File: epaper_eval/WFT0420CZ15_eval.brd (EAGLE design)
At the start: 47 x 47 mm, 15 parts, among them CN1 WFT0420CZ15_IF, CN2 WFT0420CZ15

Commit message: 部品を追加
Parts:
- added C10, C12: 1uF50V, Parts:SMD_2012
- added C11: 4.7uF50V, Parts:SMD_2012
- added C13: 0.1uF, Parts:SMD_2012
- added D1, D2, D3: MBR0530, Parts:MBR0530
- added L1: 10uH, Parts:NLCV25T
- added Q1: SI1308EDL, Parts:SOT323
- added R1: 0.47, Parts:SMD_2012
- added R2, R3: 4.7k, Parts:SMD_2012
- added U1: LM75BIMM-3, Parts:SSOP8-DGK
- C9: device Parts:C1210 -> Parts:SMD_2012
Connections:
- new net GDR: CN2.2, Q1.1
- new net N$15: C11.2, D2.2, D3.1
- new net N$6: C11.1, D1.2, L1.2, Q1.3
- new net PREVGH: C10.1, CN2.21, D1.1
- new net PREVGL: C12.1, CN2.23, D3.2
- new net RESE: CN2.3, Q1.2, R1.2
- new net TSCL: CN2.6, R3.1, U1.2
- new net TSDA: CN2.7, R2.1, U1.1
- net +3V3: now also C13.1, L1.1, R2.2, R3.2, U1.8
- net 0V: now also C10.2, C12.2, C13.2, D2.1, R1.1, U1.4, U1.5, U1.6, U1.7

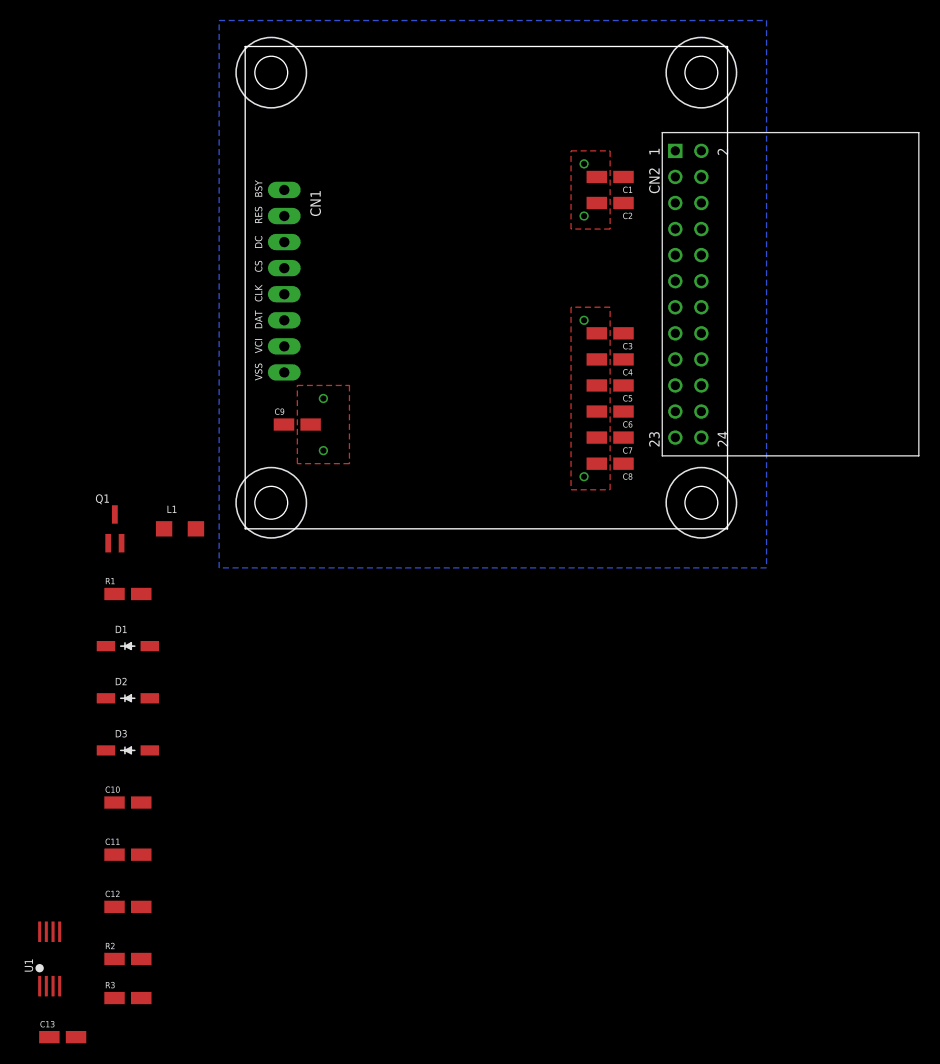
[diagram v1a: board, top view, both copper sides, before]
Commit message: レイアウト変更
概ね確定です
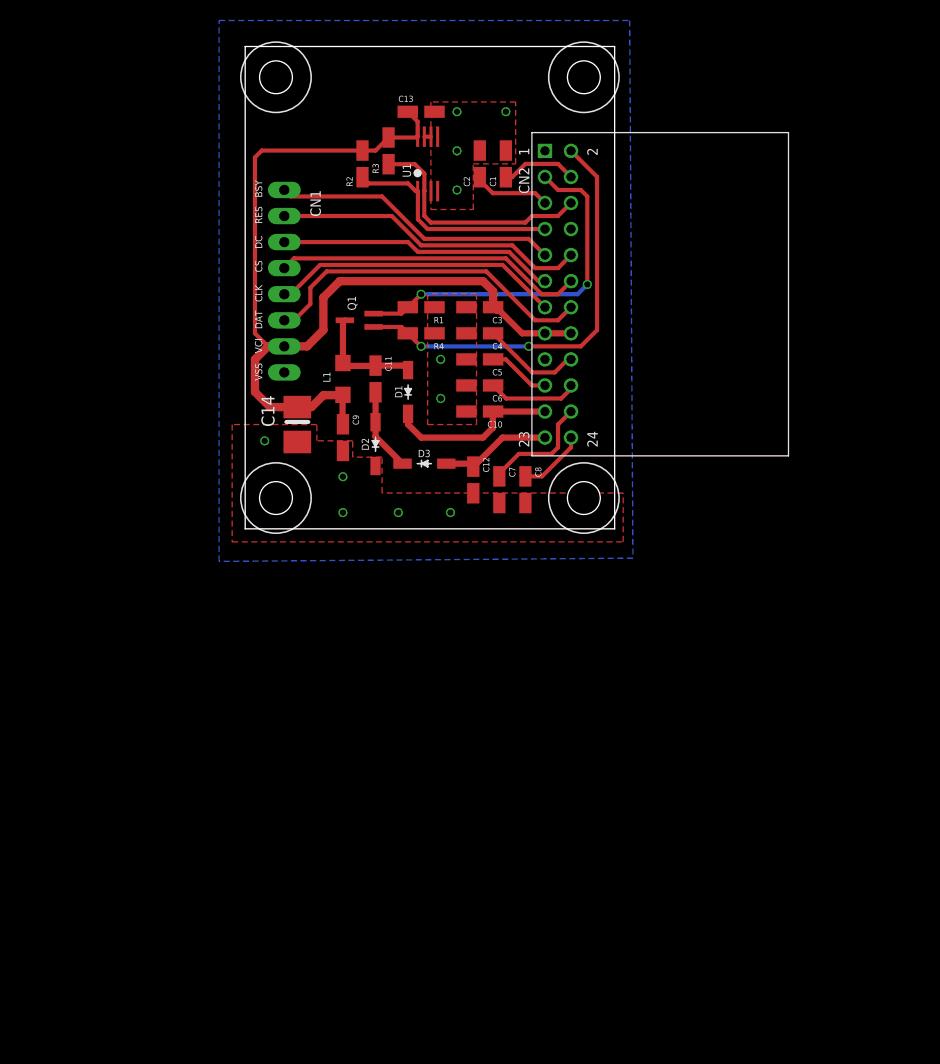
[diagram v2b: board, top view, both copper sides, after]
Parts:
- added C14: 10uF16V, Parts:C1210
- added R4: 100k, Parts:SMD_2012
- moved C13 96.7 mm to (17.1, 40.6)
- moved R3 86.4 mm to (14.0, 36.8), turned to 90 degrees
- moved U1 85.8 mm to (17.8, 35.6)
- moved R2 80.8 mm to (11.4, 35.6), turned to 90 degrees
- moved C12 53.5 mm to (22.2, 4.76), turned to 270 degrees
- moved C11 52.3 mm to (12.7, 14.6), turned to 270 degrees
- moved C10 51.3 mm to (22.9, 11.4), turned to 180 degrees
- moved D3 40.2 mm to (17.5, 6.35)
- moved R1 40.0 mm to (17.1, 21.6), turned to 180 degrees
- moved D1 36.9 mm to (15.9, 13.3), turned to 90 degrees
- moved D2 34.6 mm to (12.7, 8.26), turned to 90 degrees
- moved Q1 31.3 mm to (11.1, 20.3), turned to 90 degrees
- moved L1 21.6 mm to (9.53, 14.6), turned to 90 degrees
- moved C2 13.3 mm to (22.9, 35.6), turned to 90 degrees
- moved C3 13.0 mm to (22.9, 21.6)
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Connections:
- net +3V3: now also C14.1
- net 0V: now also C14.2, R4.1
- net GDR: now also R4.2
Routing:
- net +3V3: track 0.00 -> 93.0 mm
- net GDR: track 0.00 -> 41.7 mm, vias 0 -> 2
- net RESE: track 0.00 -> 35.5 mm, vias 0 -> 2
- net N$14: track 0.00 -> 33.3 mm
- net N$10: track 0.00 -> 30.6 mm
- net N$12: track 0.00 -> 30.3 mm
- net N$13: track 0.00 -> 28.3 mm
- net N$9: track 0.00 -> 28.0 mm
- net N$11: track 0.00 -> 27.0 mm
- net TSCL: track 0.00 -> 23.3 mm
- net TSDA: track 0.00 -> 21.5 mm
- net PREVGH: track 0.00 -> 16.9 mm
- net N$2: track 0.00 -> 11.1 mm
- net PREVGL: track 0.00 -> 10.9 mm
- net N$6: track 0.00 -> 10.9 mm
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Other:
- board size 47 x 47 mm -> 36 x 47 mm
